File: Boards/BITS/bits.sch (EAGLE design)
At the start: 25 parts, among them T1 Si1013, X1 22-23-2021, X2 53398-10, X3 22-23-2031, X4 22-23-2041

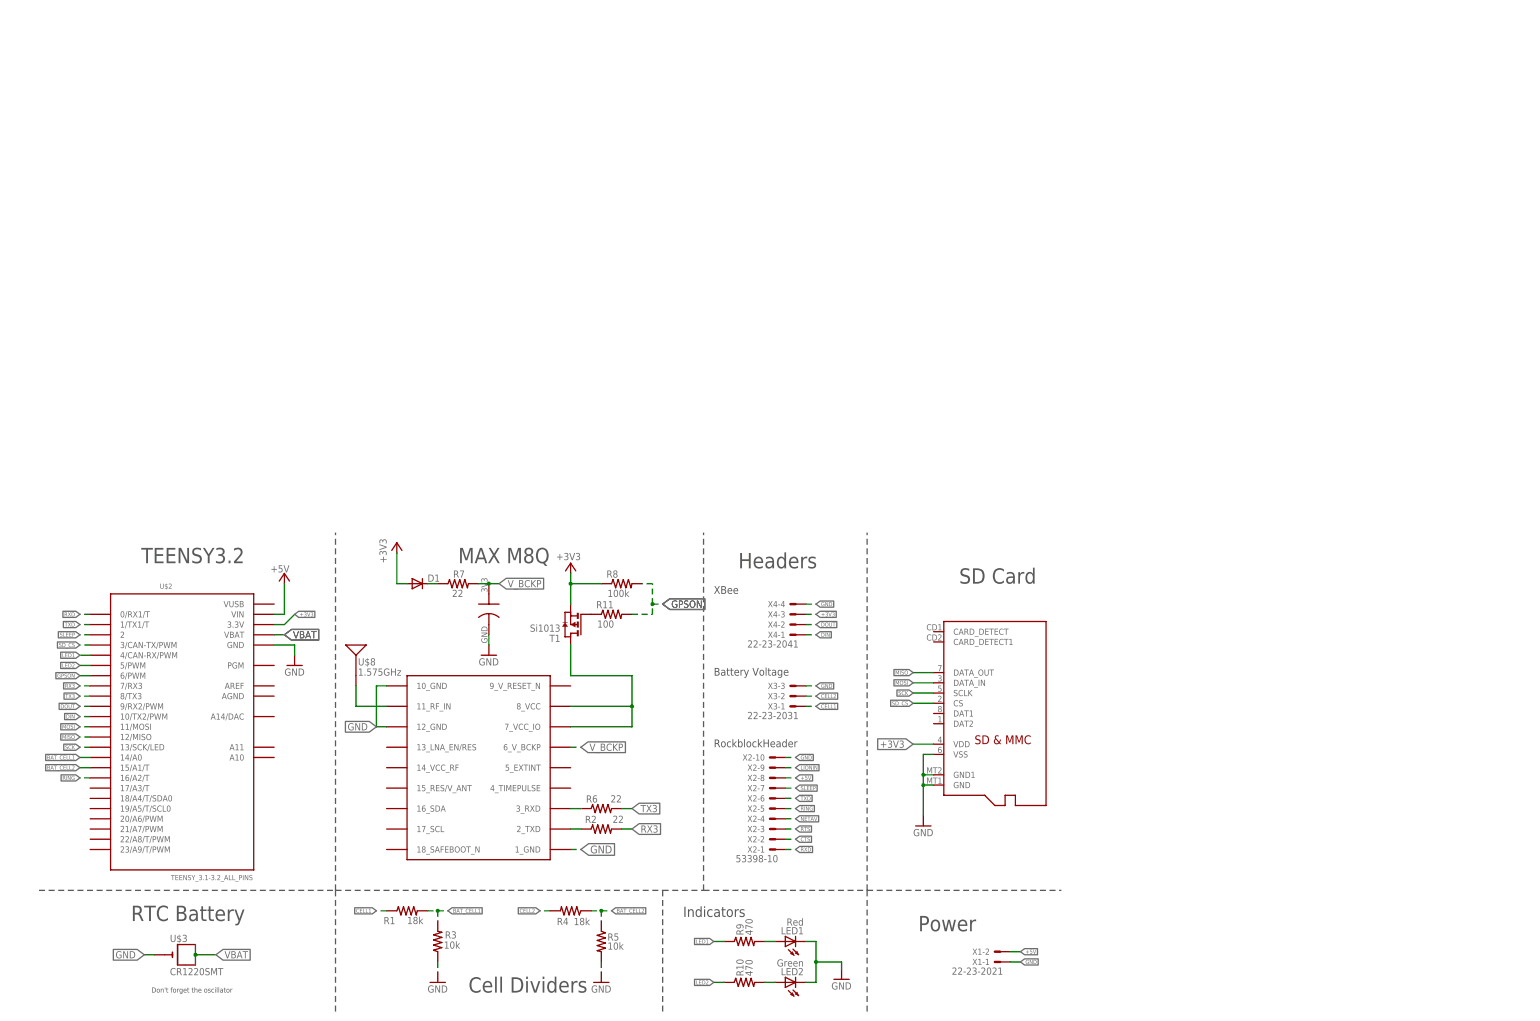
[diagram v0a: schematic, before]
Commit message: Cleaned up the BITS schematic
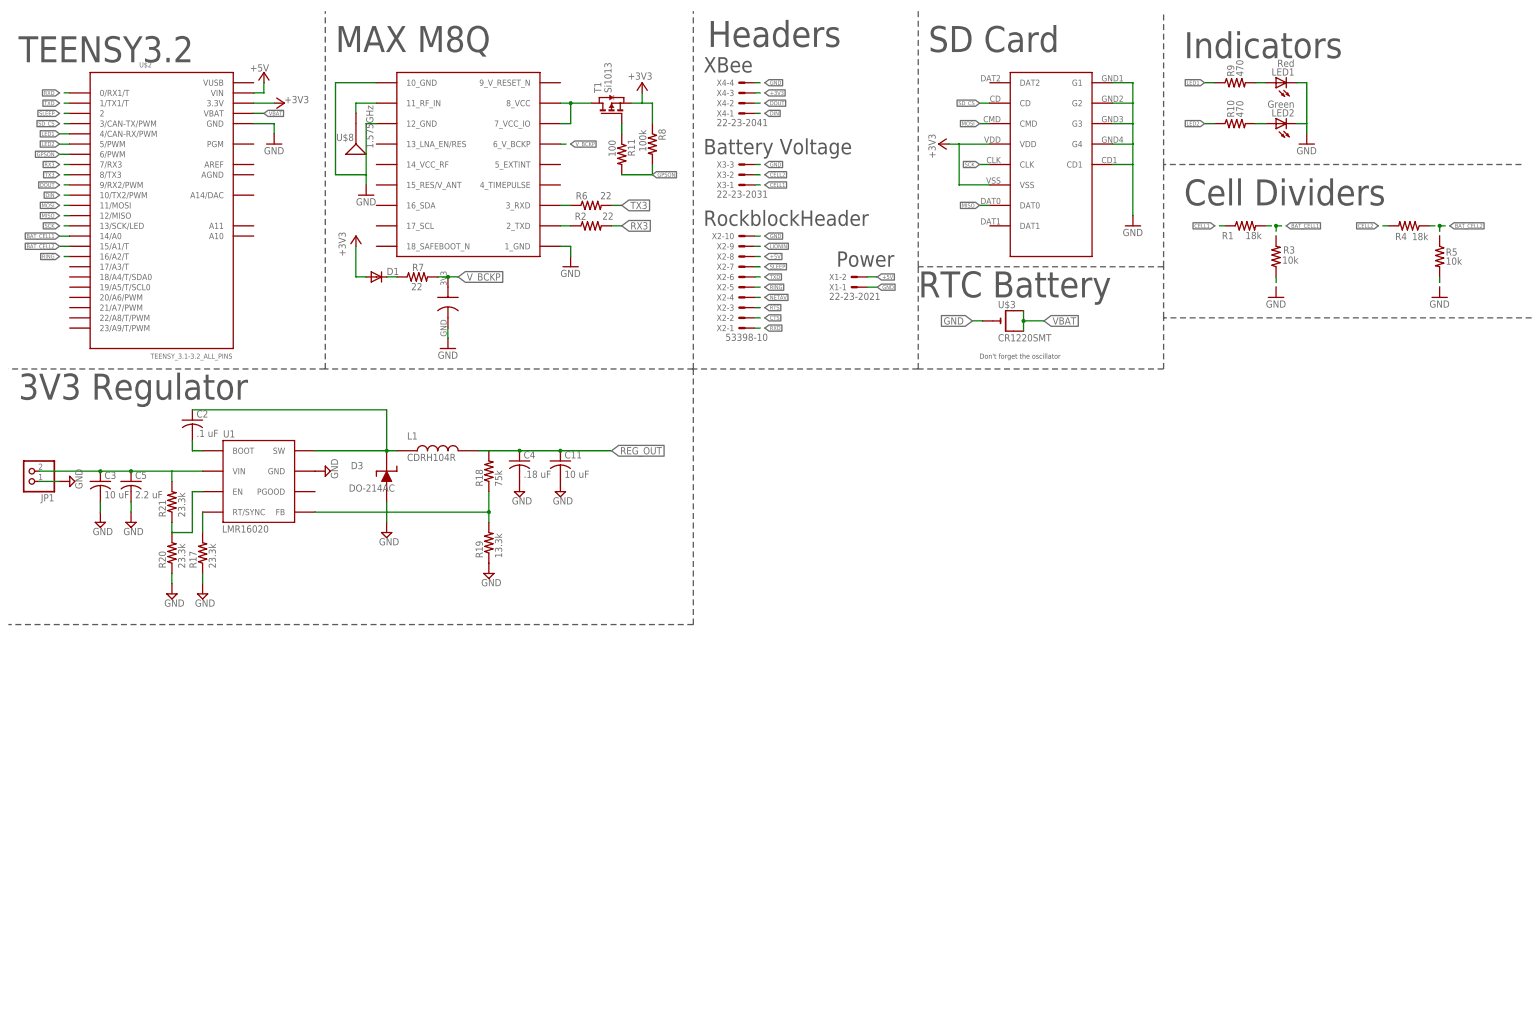
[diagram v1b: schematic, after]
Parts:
- removed U$1: MICROSD, adafruit:MICROSD
- added C11: 10 uF, resistor:C-USC0603
- added C2: .1 uF, resistor:C-USC0603
- added C3: 10 uF, resistor:C-USC1210
- added C4: .18 uF, resistor:C-USC0603
- added C5: 2.2 uF, resistor:C-USC1210
- added D3: DO-214AC, HASP:DO-214AC
- added JP1: (no value), pinhead:PINHD-1X2
- added L1: CDRH104R, library:CDRH104R
- added R17, R20, R21: 23.3k, resistor:R-US_R0603
- added R18: 75k, resistor:R-US_R0603
- added R19: 13.3k, resistor:R-US_R0603
- added U$4: MICRO_SD, NR_connectors:MICRO_SD
- added U1: LMR16020, HASP:LMR16020
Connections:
- new net IN1: C3.1, C5.1, JP1.2, R21.2, U1.VIN
- new net N$29: R17.2, U1.RT/SYNC
- new net N$31: C2.2, U1.BOOT
- new net N$32: C2.1, D3.P$2, L1.P$1, U1.SW
- new net N$33: R18.1, R19.2, U1.FB
- new net N$34: R20.2, R21.1, U1.EN
- new net REG_OUT: C11.1, C4.1, L1.P$2, R18.2
- net +3V3: now also U$4.VDD, U$4.VSS; no longer U$1.VDD
- net GND: now also C11.2, C3.2, C4.2, C5.2, D3.P$1, JP1.1, R17.1, R19.1, R20.1, U$4.CD1, U$4.G1, U$4.G2, U$4.G3, U$4.G4, U1.GND; no longer U$1.GND, U$1.GND1, U$1.VSS
- net MISO: now also U$4.DAT0; no longer U$1.DATA_OUT
- net MOSI: now also U$4.CMD; no longer U$1.DATA_IN
- net SCK: now also U$4.CLK; no longer U$1.SCLK
- net SD_CS: now also U$4.CD; no longer U$1.CS
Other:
- note added: "3V3 Regulator"
- moved on the sheet: D1, LED1, LED2, R1, R10, R11, R2, R3, R4, R5, R6, R7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

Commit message: Revert "reverted bits schematic back to my last commit""
This reverts commit d8380e26c9c134d67ee78542be9b2ca2b8e420f0.
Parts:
- removed R8: 100k, rcl:R-US_R0603
- T1: value Si1013 -> SI1013; device zetex:PMOSSOT23 -> cmdLibs:SI1013; SPICEPREFIX J -> (none)
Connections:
- removed net LIONIN: X2-9.S
- removed net REG_OUT: C11.1, C4.1, L1.P$2, R18.2
- net +3V3: now also C11.1, C4.1, L1.P$2, R18.2, X2-9.S; no longer R8.1
- net +5V: no longer U$2.VIN
- net GPSON: no longer R8.2
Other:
- moved on the sheet: D1, LED1, LED2, R10, R11, R2, R6, R7, R9, U$3, U$8

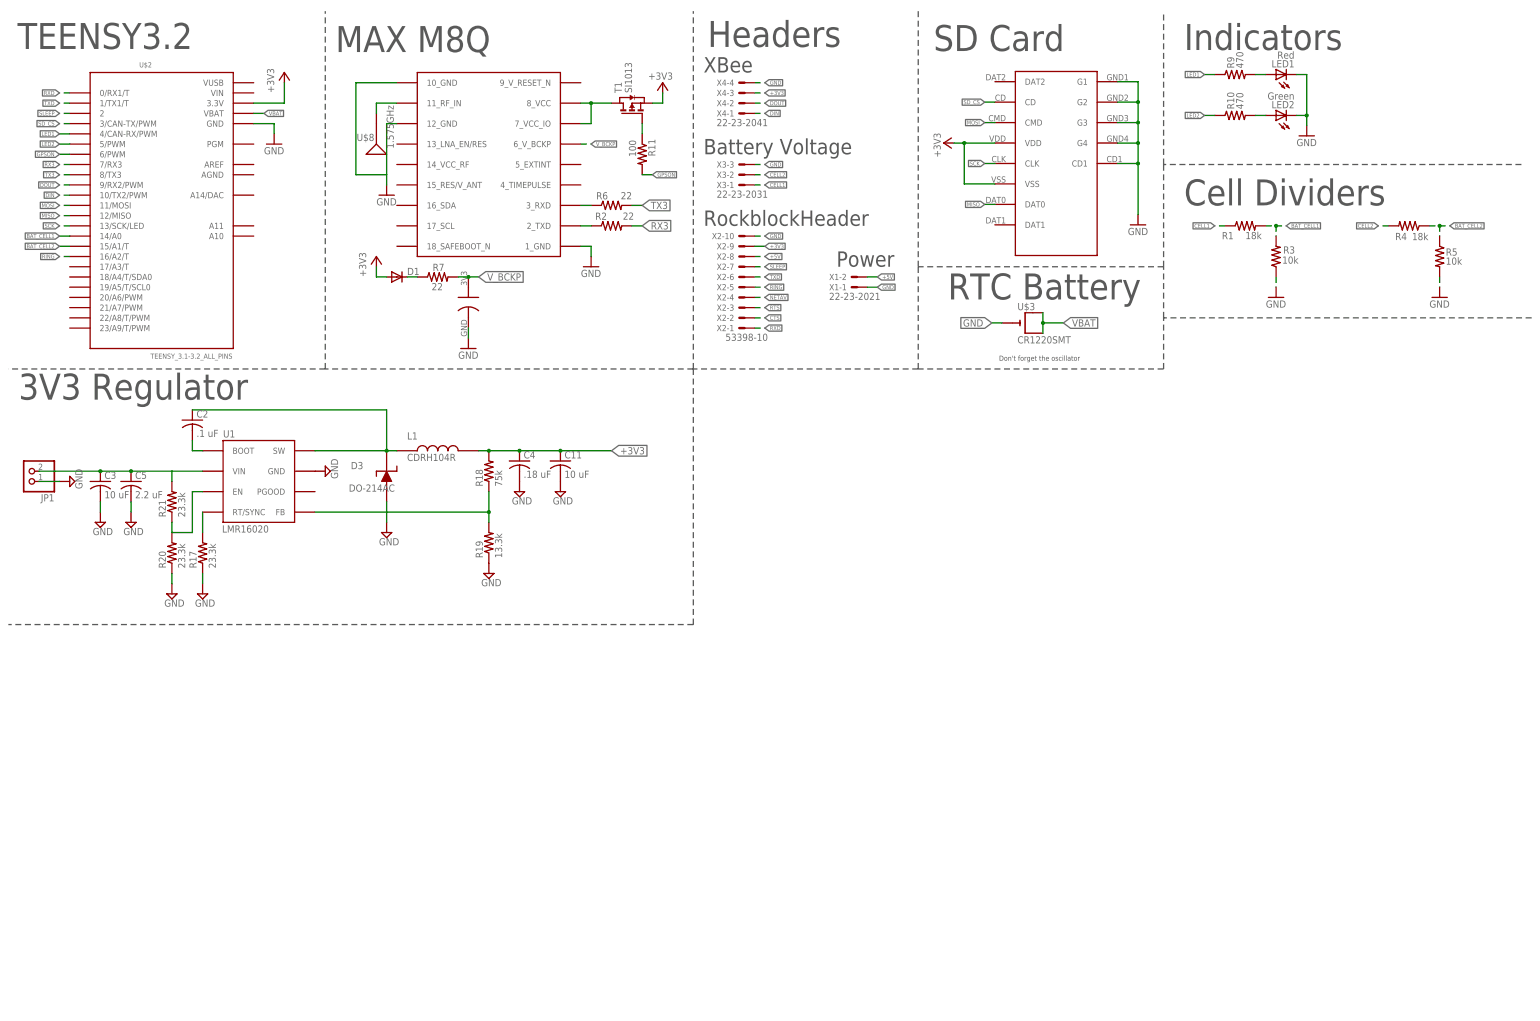
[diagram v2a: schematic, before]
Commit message: reverted bits schematic back to my last commit"
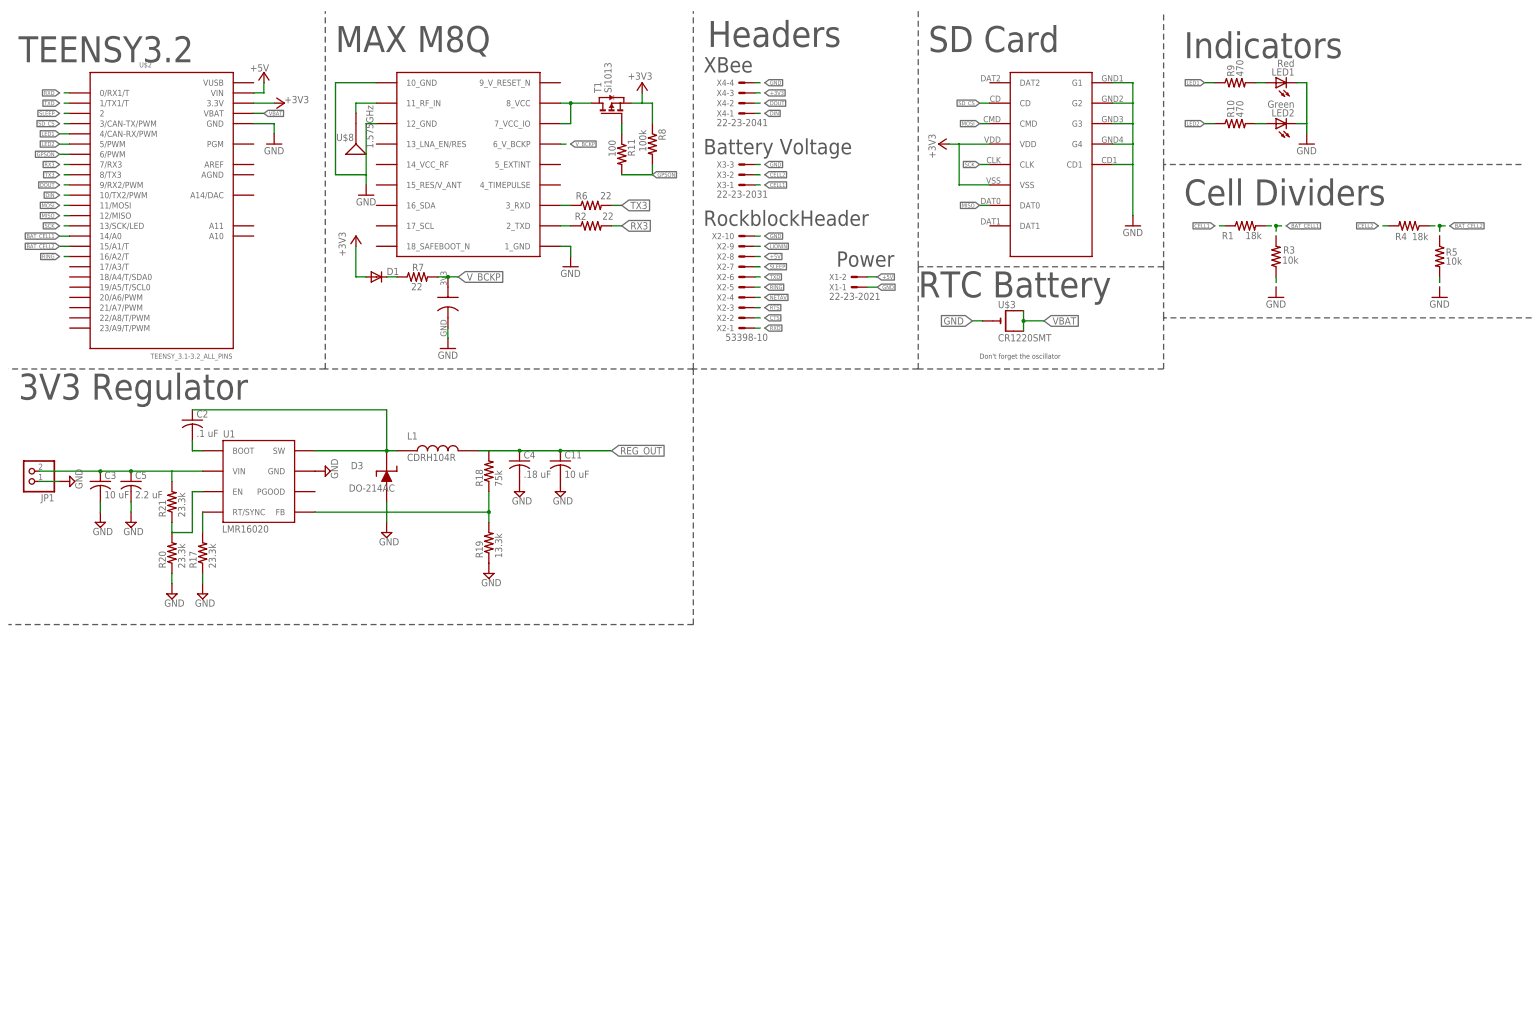
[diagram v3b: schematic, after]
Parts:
- added R8: 100k, rcl:R-US_R0603
- T1: value SI1013 -> Si1013; device cmdLibs:SI1013 -> zetex:PMOSSOT23; SPICEPREFIX (none) -> J
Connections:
- new net LIONIN: X2-9.S
- new net REG_OUT: C11.1, C4.1, L1.P$2, R18.2
- net +3V3: now also R8.1; no longer C11.1, C4.1, L1.P$2, R18.2, X2-9.S
- net +5V: now also U$2.VIN
- net GPSON: now also R8.2
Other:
- moved on the sheet: D1, LED1, LED2, R10, R11, R2, R6, R7, R9, U$3, U$8
